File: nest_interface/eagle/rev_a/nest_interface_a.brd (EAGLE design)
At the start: 133.3 x 110.5 mm, 127 parts, among them J1 MOLEX_MICRO_USB_B_047346, J10 CONN_BLOCK_2, J11 CONN_BLOCK_2, J12 CONN_BLOCK_2, J13 CONN_BLOCK_2, J14 CONN_BLOCK_3, J15 CONN_BLOCK_3, J16 CONN_BLOCK_7, J17 CONN_BLOCK_7, J18 CONN_BLOCK_8, J19 CONN_BLOCK_8, J2 MOLEX_MICRO_USB_B_047346, J20 CONN_BLOCK_8, J21 CONN_BLOCK_8, J5 PJ-036A-SMT, J6 CONN_BLOCK_2, J7 CONN_BLOCK_2, J8 CONN_BLOCK_2, J9 CONN_BLOCK_2, U1 EPIC-CORE_A, U2 MSP430F1611IPM, U3 FT232RL, U4 FT232RL, U5 MPC1825, U6 TC1262, U7 PCA9575, U8 PCA9575, Y1 FC-135_32.768KA-A3

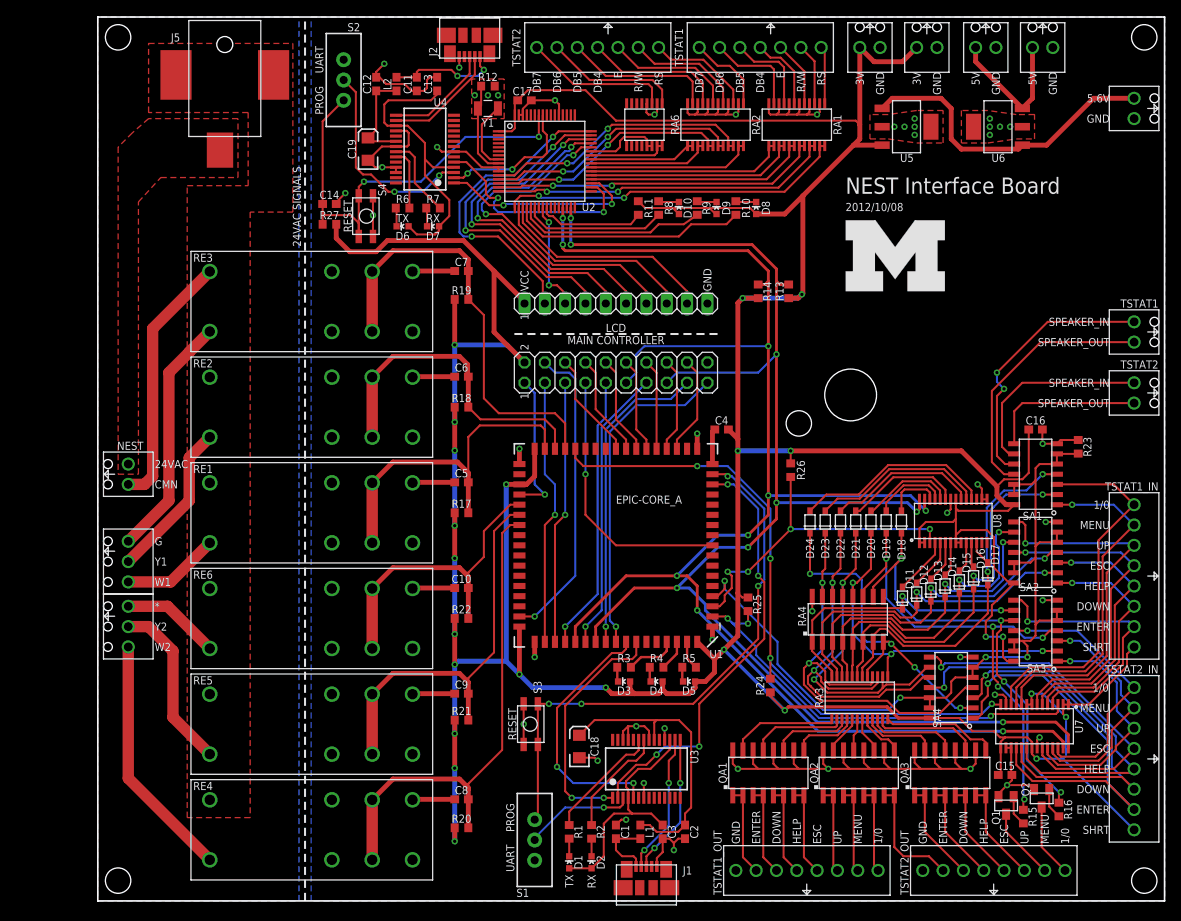
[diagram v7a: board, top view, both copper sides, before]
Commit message: slight fixes
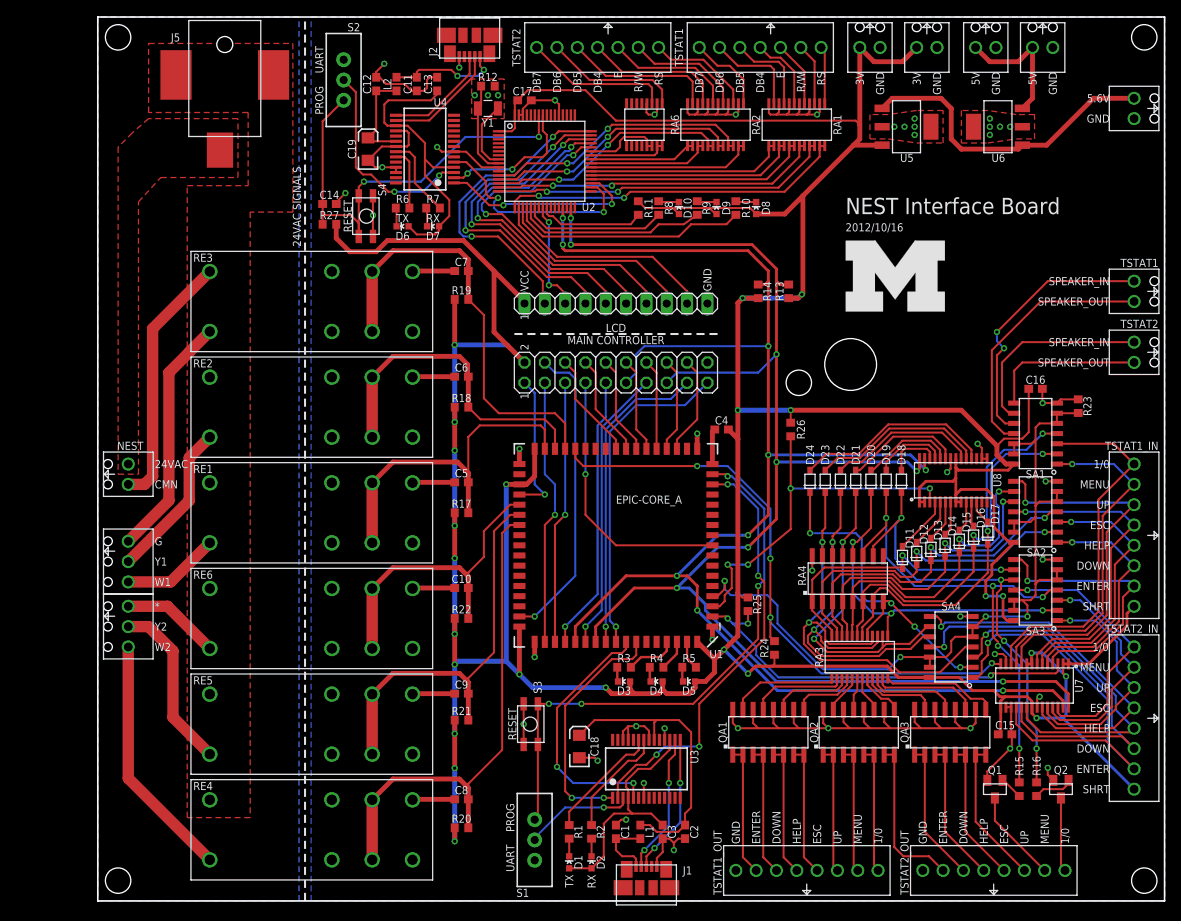
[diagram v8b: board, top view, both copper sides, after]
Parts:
- moved D11 5.08 mm to (100.6, 42.9)
- moved D14 5.08 mm to (105.9, 44.5)
- moved SA3 5.08 mm to (117.2, 38.9)
- moved U8 5.08 mm to (106.9, 52.6)
- moved QA1 5.08 mm to (83.8, 21.1)
- moved QA2 5.08 mm to (95.1, 21.1)
- moved QA3 5.08 mm to (106.6, 21.1)
- moved RA3 5.08 mm to (95.2, 30.5)
- moved C15 5.08 mm to (113.4, 20.8)
- moved C16 5.08 mm to (117.2, 64.0)
- moved D12 5.08 mm to (102.4, 43.4)
- moved D13 5.08 mm to (104.1, 43.9)
- moved D15 5.08 mm to (107.7, 45.0)
- moved D16 5.08 mm to (109.5, 45.5)
- moved D17 5.08 mm to (111.3, 46.0)
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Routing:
- net TSTAT2_UP_OUT: track 12.7 -> 18.3 mm
- net TSTAT_OUT_I2C_RST: track 41.7 -> 47.1 mm
- net TSTAT2_ENTER_OUT: track 15.1 -> 20.1 mm
- net TSTAT2_ESC_OUT: track 12.7 -> 17.7 mm
- net TSTAT1_HELP_OUT: track 11.4 -> 16.4 mm
- net TSTAT1_ENTER_OUT: track 11.4 -> 16.4 mm
- net TSTAT1_UP_OUT: track 10.9 -> 16.0 mm
- net TSTAT1_ON/OFF_OUT: track 10.9 -> 16.0 mm
- net TSTAT1_MENU_OUT: track 10.9 -> 16.0 mm
- net TSTAT1_ESC_OUT: track 11.4 -> 16.4 mm
- net TSTAT1_DOWN_OUT: track 11.4 -> 16.4 mm
- net TSTAT2_HELP_OUT: track 12.7 -> 17.7 mm
- net TSTAT2_DOWN_OUT: track 12.7 -> 17.7 mm
- net TSTAT_IN_I2C_INT: track 82.0 -> 77.5 mm
- net VCC: track 586.6 -> 583.4 mm
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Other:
- board text added: "2012/10/16"
- board text removed: "2012/10/08"
